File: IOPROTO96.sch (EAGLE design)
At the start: 5 parts

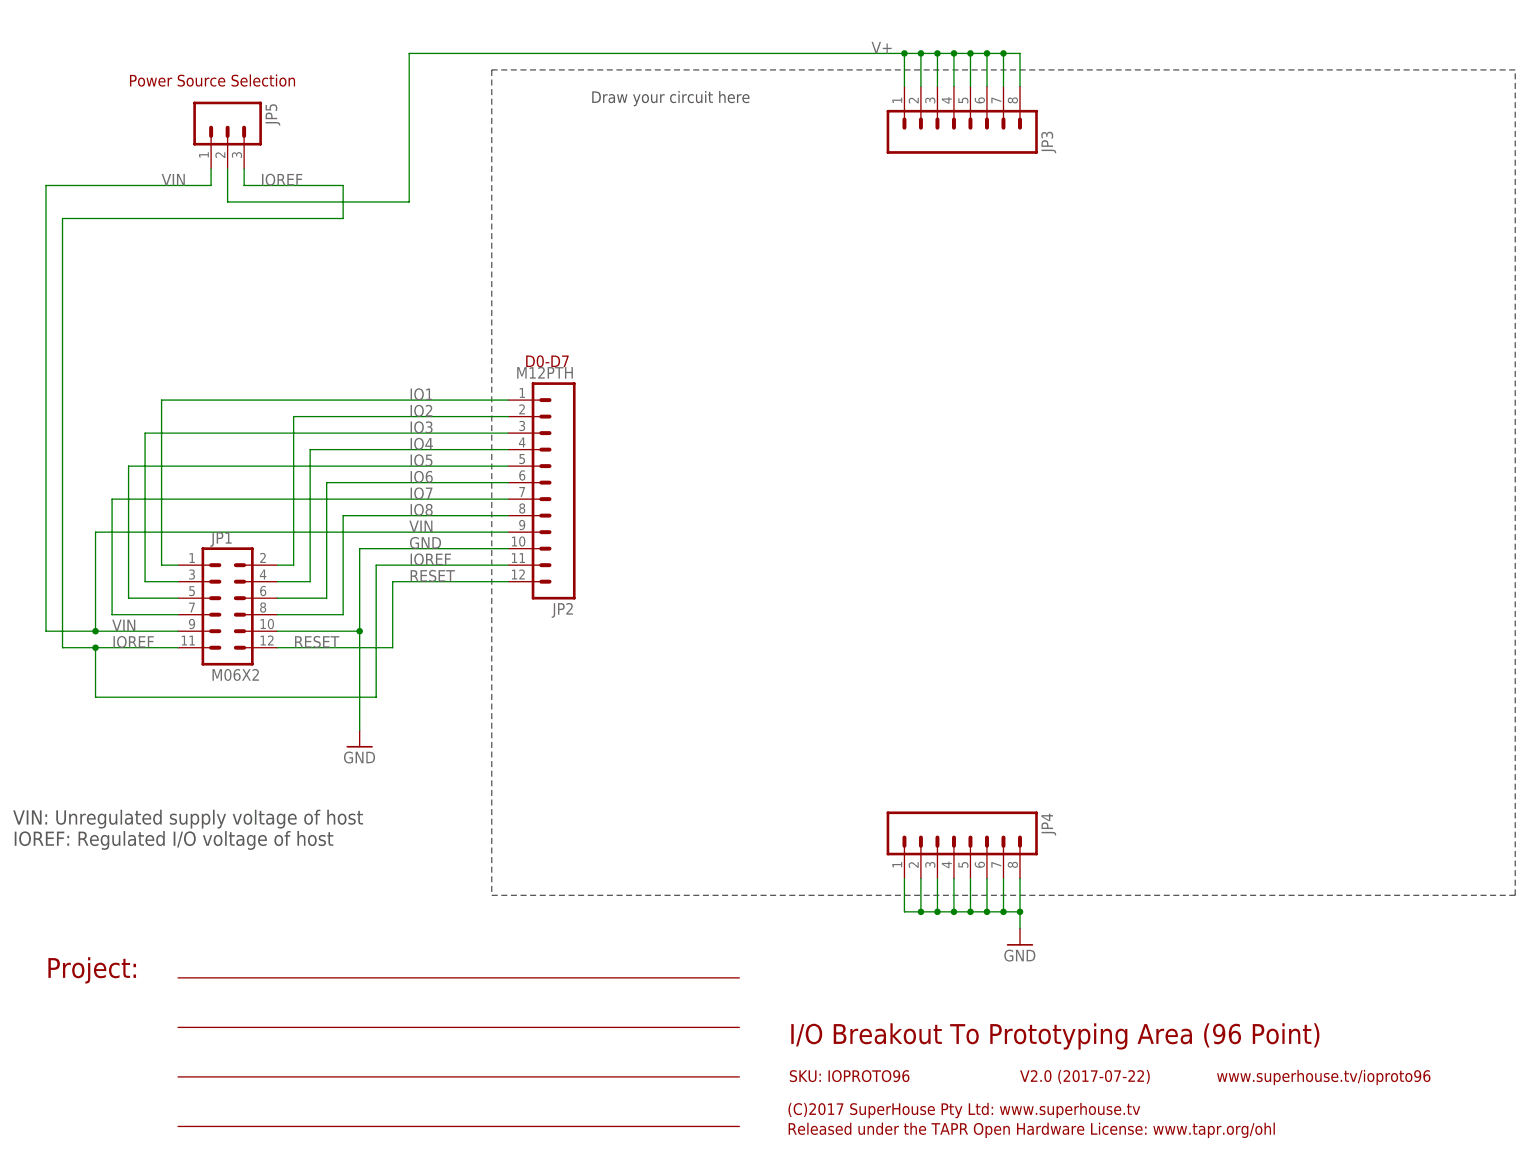
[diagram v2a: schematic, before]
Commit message: Part replacement using SuperHouse libraries
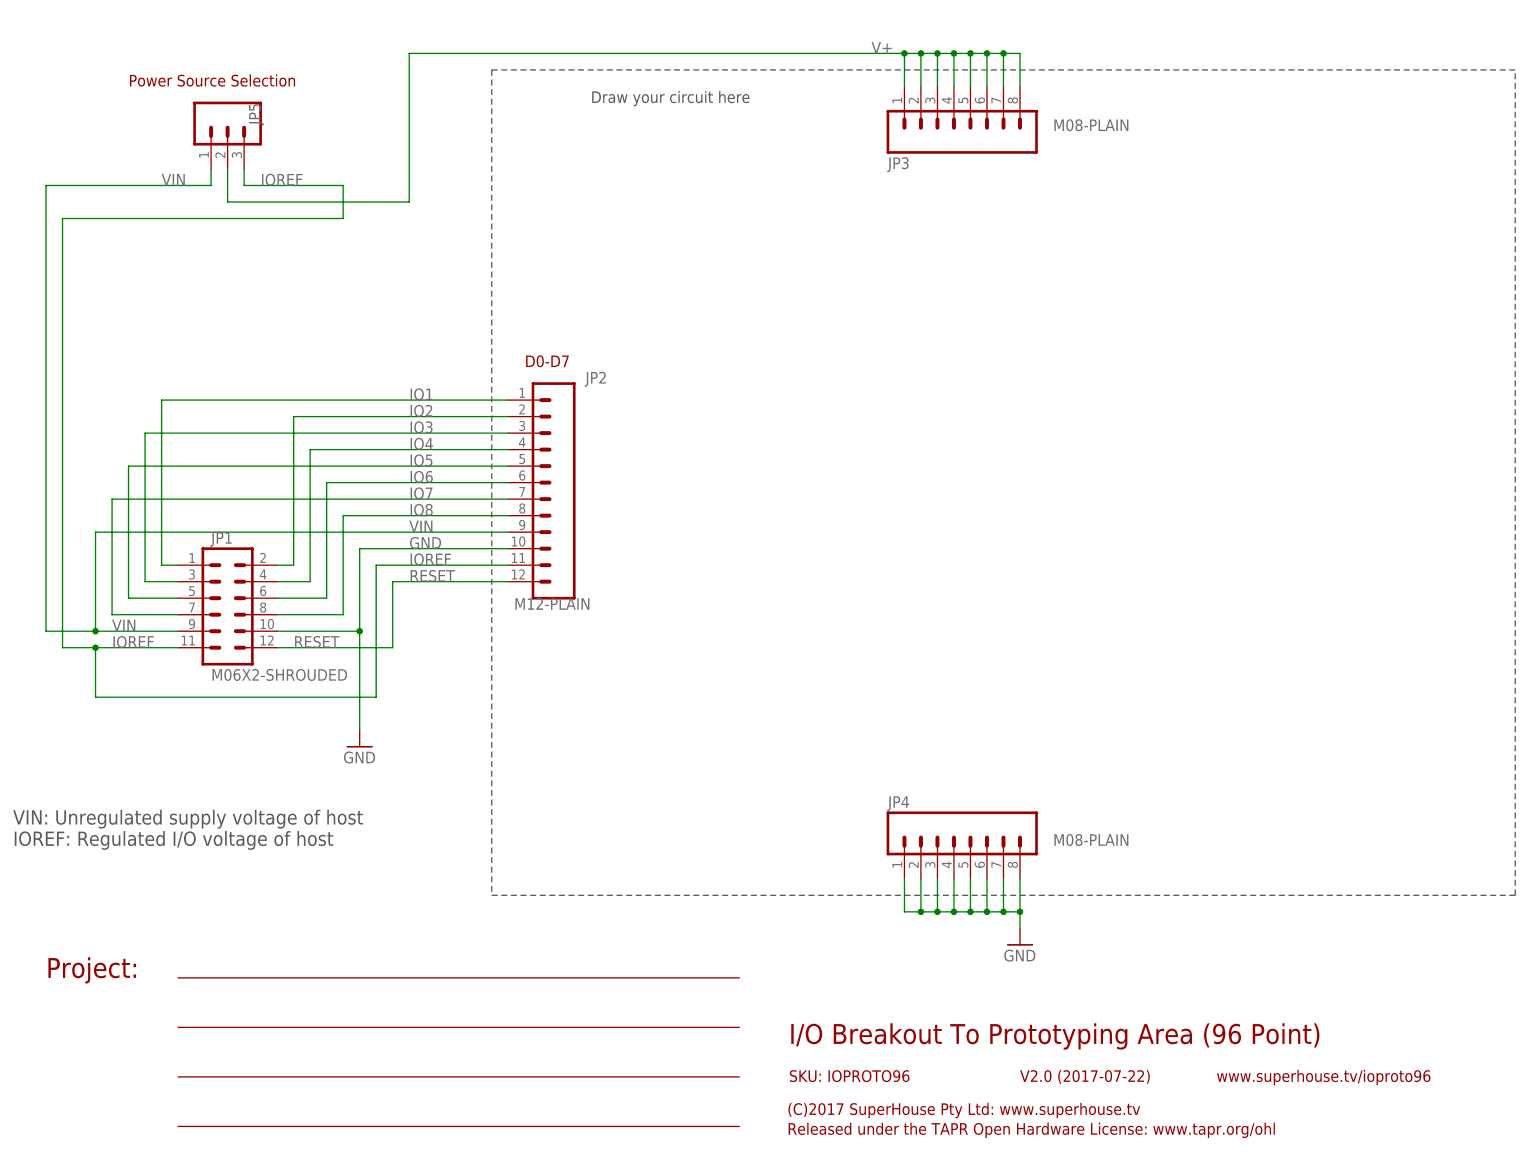
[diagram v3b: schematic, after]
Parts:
- JP1: value M06X2 -> M06X2-SHROUDED; device freetronics-jon:M06X2 -> SuperHouse-Connectors:M06X2-SHROUDED
- JP2: value M12PTH -> M12-PLAIN; device freetronics-original:M12PTH -> SuperHouse-Connectors:M12-PLAIN
- JP3, JP4: value (none) -> M08-PLAIN; device freetronics-master-v1:M08 -> SuperHouse-Connectors:M08-PLAIN
- JP5: device freetronics-jon:M03PTH -> SuperHouse-Connectors:M03-PIN
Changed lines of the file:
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@@
 <?xml version="1.0" encoding="utf-8"?>
 <!DOCTYPE eagle SYSTEM "eagle.dtd">
-<eagle version="6.5.0">
+<eagle version="9.4.2">
 <drawing>
 <settings>
-<setting alwaysvectorfont="yes"/>
+<setting alwaysvectorfont="no"/>
+<setting keepoldvectorfont="yes"/>
 <setting verticaltext="up"/>
 </settings>
@@
 <layer number="59" name="tCarbon" color="7" fill="1" visible="no" active="no"/>
 <layer number="60" name="bCarbon" color="7" fill="1" visible="no" active="no"/>
+<layer number="61" name="pt_docu" color="7" fill="0" visible="no" active="no"/>
+<layer number="88" name="SimResults" color="9" fill="1" visible="yes" active="yes"/>
+<layer number="89" name="SimProbes" color="9" fill="1" visible="yes" active="yes"/>
 <layer number="90" name="Modules" color="7" fill="1" visible="yes" active="yes"/>
 <layer number="91" name="Nets" color="2" fill="1" visible="yes" active="yes"/>
@@
 <layer number="112" name="tSilk" color="7" fill="1" visible="yes" active="yes"/>
 <layer number="113" name="ReferenceLS" color="7" fill="1" visible="no" active="no"/>
+<layer number="114" name="FRNTMAAT1" color="7" fill="1" visible="yes" active="yes"/>
+<layer number="115" name="FRNTMAAT2" color="7" fill="1" visible="yes" active="yes"/>
 <layer number="116" name="Patch_BOT" color="9" fill="4" visible="yes" active="yes"/>
+<layer number="117" name="BACKMAAT1" color="7" fill="1" visible="yes" active="yes"/>
 <layer number="118" name="Rect_Pads" color="7" fill="1" visible="no" active="no"/>
+<layer number="119" name="KAP_TEKEN" color="7" fill="1" visible="yes" active="yes"/>
+<layer number="120" name="KAP_MAAT1" color="7" fill="1" visible="yes" active="yes"/>
 <layer number="121" name="_tsilk" color="7" fill="1" visible="yes" active="yes"/>
 <layer number="122" name="_bsilk" color="7" fill="1" visible="yes" active="yes"/>
@@
 <layer number="128" name="_bValues" color="7" fill="1" visible="yes" active="yes"/>
 <layer number="129" name="Mask" color="7" fill="1" visible="yes" active="yes"/>
+<layer number="130" name="SMDSTROOK" color="7" fill="1" visible="yes" active="yes"/>
 <layer number="131" name="tAdjust" color="7" fill="1" visible="yes" active="yes"/>
 <layer number="132" name="bAdjust" color="7" fill="1" visible="yes" active="yes"/>
+<layer number="133" name="bottom_silk" color="7" fill="1" visible="yes" active="yes"/>
+<layer number="134" name="silk_top" color="7" fill="1" visible="no" active="no"/>
+<layer number="135" name="silk_bottom" color="7" fill="1" visible="no" active="no"/>
+<layer number="136" name="silktop" color="7" fill="1" visible="yes" active="yes"/>
+<layer number="137" name="silkbottom" color="7" fill="1" visible="yes" active="yes"/>
+<layer number="138" name="GND@2" color="7" fill="1" visible="yes" active="yes"/>
+<layer number="139" name="mtKeepout" color="7" fill="1" visible="yes" active="yes"/>
+<layer number="140" name="mbKeepout" color="7" fill="1" visible="yes" active="yes"/>
+<layer number="141" name="mtRestrict" color="7" fill="1" visible="yes" active="yes"/>
+<layer number="142" name="mbRestrict" color="7" fill="1" visible="yes" active="yes"/>
+<layer number="143" name="mvRestrict" color="7" fill="1" visible="yes" active="yes"/>
 <layer number="144" name="Drill_legend" color="7" fill="1" visible="yes" active="yes"/>
+<layer number="145" name="DrillLegend_01-16" color="7" fill="1" visible="yes" active="yes"/>
+<layer number="146" name="p_Milling" color="3" fill="9" visible="yes" active="yes"/>
+<layer number="147" name="COVER" color="14" fill="1" visible="yes" active="yes"/>
+<layer number="148" name="mDocument" color="7" fill="1" visible="yes" active="yes"/>
+<layer number="149" name="mReference" color="7" fill="1" visible="yes" active="yes"/>
 <layer number="150" name="Notes" color="7" fill="1" visible="yes" active="yes"/>
 <layer number="151" name="HeatSink" color="7" fill="1" visible="yes" active="yes"/>
@@
 <layer number="154" name="FabDoc2" color="2" fill="1" visible="no" active="no"/>
 <layer number="155" name="FabDoc3" color="7" fill="15" visible="no" active="no"/>
+<layer number="166" name="AntennaArea" color="7" fill="1" visible="yes" active="yes"/>
+<layer number="168" name="4mmHeightArea" color="7" fill="1" visible="yes" active="yes"/>
+<layer number="190" name="Comments" color="12" fill="1" visible="yes" active="yes"/>
+<layer number="191" name="mNets" color="7" fill="1" visible="yes" active="yes"/>
+<layer number="192" name="mBusses" color="7" fill="1" visible="yes" active="yes"/>
+<layer number="193" name="mPins" color="7" fill="1" visible="yes" active="yes"/>
+<layer number="194" name="mSymbols" color="7" fill="1" visible="yes" active="yes"/>
+<layer number="195" name="mNames" color="7" fill="1" visible="yes" active="yes"/>
+<layer number="196" name="mValues" color="7" fill="1" visible="yes" active="yes"/>
 <layer number="199" name="Contour" color="7" fill="1" visible="yes" active="yes"/>
 <layer number="200" name="200bmp" color="1" fill="10" visible="no" active="no"/>
@@
 </classes>
 <parts>
-<part name="JP1" library="freetronics-jon" deviceset="M06X2" device=""/>
+<part name="JP1" library="SuperHouse-Connectors" library_urn="urn:adsk.eagle:library:11765989" deviceset="M06X2" device="-SHROUDED" package3d_urn="urn:adsk.eagle:package:11976015/2"/>
 <part name="GND1" library="freetronics" deviceset="GND" device=""/>
-<part name="JP2" library="freetronics-original" deviceset="M12" device="PTH"/>
-<part name="JP3" library="freetronics-master-v1" deviceset="M08" device=""/>
-<part name="JP4" library="freetronics-master-v1" deviceset="M08" device=""/>
+<part name="JP2" library="SuperHouse-Connectors" library_urn="urn:adsk.eagle:library:11765989" deviceset="M12" device="-PLAIN" package3d_urn="urn:adsk.eagle:package:12194678/1"/>
+<part name="JP3" library="SuperHouse-Connectors" library_urn="urn:adsk.eagle:library:11765989" deviceset="M08" device="-PLAIN" package3d_urn="urn:adsk.eagle:package:11866882/1"/>
+<part name="JP4" library="SuperHouse-Connectors" library_urn="urn:adsk.eagle:library:11765989" deviceset="M08" device="-PLAIN" package3d_urn="urn:adsk.eagle:package:11866882/1"/>
 <part name="GND2" library="freetronics" deviceset="GND" device=""/>
-<part name="JP5" library="freetronics-jon" deviceset="M03" device="PTH"/>
+<part name="JP5" library="SuperHouse-Connectors" library_urn="urn:adsk.eagle:library:11765989" deviceset="M03" device="-PIN" package3d_urn="urn:adsk.eagle:package:11815967/3"/>
 </parts>
 <sheets>
@@
 </plain>
 <instances>
-<instance part="JP1" gate="G$1" x="38.1" y="88.9"/>
-<instance part="GND1" gate="1" x="58.42" y="66.04"/>
-<instance part="JP2" gate="G$1" x="91.44" y="104.14" rot="R180"/>
-<instance part="JP3" gate="G$1" x="149.86" y="162.56" rot="MR90"/>
-<instance part="JP4" gate="G$1" x="149.86" y="50.8" rot="R270"/>
-<instance part="GND2" gate="1" x="160.02" y="35.56"/>
-<instance part="JP5" gate="G$1" x="38.1" y="162.56" rot="R270"/>
+<instance part="JP1" gate="G$1" x="38.1" y="88.9" smashed="yes">
+<attribute name="VALUE" x="35.56" y="76.2" size="1.778" layer="96"/>
+<attribute name="NAME" x="35.56" y="97.282" size="1.778" layer="95"/>
+</instance>
+<instance part="GND1" gate="1" x="58.42" y="66.04" smashed="yes">
+<attribute name="VALUE" x="55.88" y="63.5" size="1.778" layer="96"/>
+</instance>
+<instance part="JP2" gate="G$1" x="88.9" y="119.38" smashed="yes" rot="R180">
+<attribute name="VALUE" x="93.98" y="88.9" size="1.778" layer="96" rot="R180"/>
+<attribute name="NAME" x="96.52" y="123.698" size="1.778" layer="95" rot="R180"/>
+</instance>
+<instance part="JP3" gate="G$1" x="142.24" y="160.02" smashed="yes" rot="MR90">
+<attribute name="VALUE" x="165.1" y="162.56" size="1.778" layer="96" rot="MR180"/>
+<attribute name="NAME" x="139.7" y="156.718" size="1.778" layer="95" rot="MR180"/>
+</instance>
+<instance part="JP4" gate="G$1" x="142.24" y="53.34" smashed="yes" rot="R270">
+<attribute name="VALUE" x="165.1" y="50.8" size="1.778" layer="96"/>
+<attribute name="NAME" x="139.7" y="56.642" size="1.778" layer="95"/>
+</instance>
+<instance part="GND2" gate="1" x="160.02" y="35.56" smashed="yes">
+<attribute name="VALUE" x="157.48" y="33.02" size="1.778" layer="96"/>
+</instance>
+<instance part="JP5" gate="G$1" x="35.56" y="162.56" smashed="yes" rot="R270">
+<attribute name="VALUE" x="27.94" y="165.1" size="1.778" layer="96" rot="R270"/>
+<attribute name="NAME" x="41.402" y="165.1" size="1.778" layer="95" rot="R270"/>
+</instance>
 </instances>
 <busses>
@@
 which will not be processed correctly with this version.
 </note>
+<note version="8.2" severity="warning">
+Since Version 8.2, EAGLE supports online libraries. The ids
+of those online libraries will not be understood (or retained)
+with this version.
+</note>
+<note version="8.3" severity="warning">
+Since Version 8.3, EAGLE supports URNs for individual library
+assets (packages, symbols, and devices). The URNs of those assets
+will not be understood (or retained) with this version.
+</note>
+<note version="8.3" severity="warning">
+Since Version 8.3, EAGLE supports the association of 3D packages
+with devices in libraries, schematics, and board files. Those 3D
+packages will not be understood (or retained) with this version.
+</note>
 </compatibility>
